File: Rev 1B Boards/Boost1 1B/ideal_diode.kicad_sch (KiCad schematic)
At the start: 6 parts, among them Q1 BSC059N04LS6, U1 LM74700

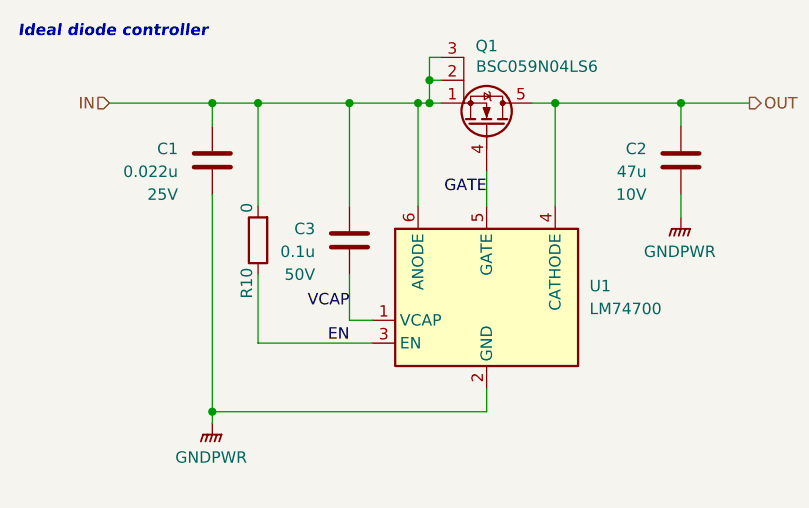
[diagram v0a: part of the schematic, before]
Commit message: Placed footprints for boost stage 1 layout
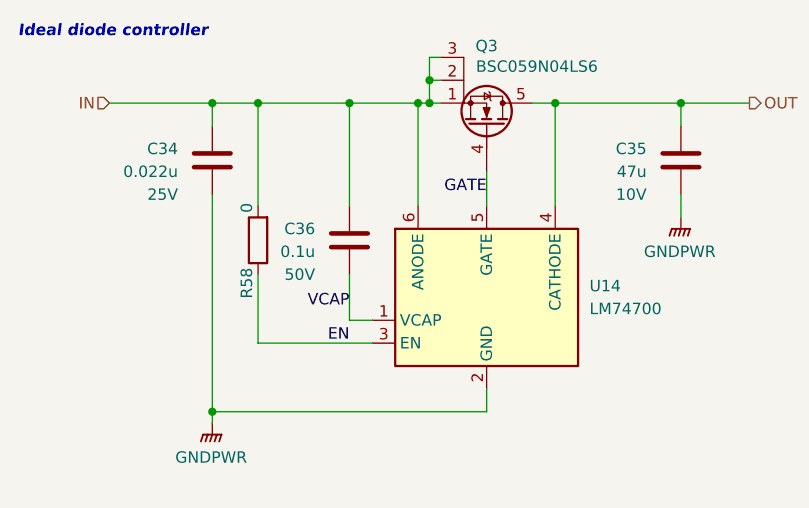
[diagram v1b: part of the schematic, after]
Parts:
- removed R10: 0, Resistor_SMD:R_0603_1608Metric_Pad0.98x0.95mm_HandSolder, symbol Device:R
- added R58: 0, Resistor_SMD:R_0603_1608Metric_Pad0.98x0.95mm_HandSolder, symbol Device:R
- renumbered C1 to C34, C2 to C35, C3 to C36, Q1 to Q3, U1 to U14
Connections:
- net EN: now also R58.1
- net IN: now also R58.2
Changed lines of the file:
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@@
+	(wire
+		(pts
+			(xy 78.74 43.18) (xy 78.74 31.75)
+		)
+		(stroke
+			(width 0)
+			(type default)
+		)
+	)
 	(wire
 		(pts
 			(xy 109.22 31.75) (xy 111.76 31.75)
-		)
-		(stroke
-			(width 0)
-			(type default)
-		)
-	)
-	(wire
-		(pts
-			(xy 78.74 43.18) (xy 78.74 31.75)
 		)
 		(stroke
@@
 			(font
 				(size 1.27 1.27)
+				(thickness 0.1588)
 			)
 			(justify right bottom)
@@
 		(on_board yes)
 		(dnp no)
-		(property "Reference" "C2"
+		(property "Reference" "C35"
 			(at 121.92 36.8299 0)
 			(effects
@@
 		)
 		(instances
-			(project "Ideal Diode Rev1"
-				(path "/1958bbb1-b715-4a10-a229-bee0eabb28b0/4a024d55-f91f-4b32-882f-0df7d5ec96e3"
-					(reference "C3")
-					(unit 1)
-				)
-			)
-			(project "Ideal Diode Rev1"
-				(path "/6197145b-e7d4-44cc-9d90-537b6501bf60/130ec867-c4fa-4318-bea9-b8fc517d0b0a"
-					(reference "C78")
-					(unit 1)
-				)
-			)
 			(project "Buck1 1B"
 				(path "/80afba09-f71a-481c-a343-2cbd993e7569/435402b6-45a2-41c3-bc2a-be9f3f280d73"
-					(reference "C2")
-					(unit 1)
-				)
-			)
-			(project "Rev 1B"
-				(path "/e5f99deb-ef42-4c5f-b80a-388477910e20/7bf219df-2692-4f86-9971-baba03c19447"
 					(reference "C35")
 					(unit 1)
@@
 		(on_board yes)
 		(dnp no)
-		(property "Reference" "C1"
+		(property "Reference" "C34"
 			(at 69.85 36.8299 0)
 			(effects
@@
 		)
 		(instances
-			(project "Ideal Diode Rev1"
-				(path "/1958bbb1-b715-4a10-a229-bee0eabb28b0/4a024d55-f91f-4b32-882f-0df7d5ec96e3"
-					(reference "C1")
-					(unit 1)
-				)
-			)
-			(project "Ideal Diode Rev1"
-				(path "/6197145b-e7d4-44cc-9d90-537b6501bf60/130ec867-c4fa-4318-bea9-b8fc517d0b0a"
-					(reference "C77")
-					(unit 1)
-				)
-			)
 			(project "Buck1 1B"
 				(path "/80afba09-f71a-481c-a343-2cbd993e7569/435402b6-45a2-41c3-bc2a-be9f3f280d73"
-					(reference "C1")
-					(unit 1)
-				)
-			)
-			(project "Rev 1B"
-				(path "/e5f99deb-ef42-4c5f-b80a-388477910e20/7bf219df-2692-4f86-9971-baba03c19447"
 					(reference "C34")
 					(unit 1)
@@
 		(dnp no)
 		(fields_autoplaced yes)
-		(property "Reference" "#PWR03"
+		(property "Reference" "#PWR095"
 			(at 73.66 72.39 0)
 			(effects
@@
 		)
 		(instances
-			(project "Ideal Diode Rev1"
-				(path "/1958bbb1-b715-4a10-a229-bee0eabb28b0/4a024d55-f91f-4b32-882f-0df7d5ec96e3"
-					(reference "#PWR0107")
-					(unit 1)
-				)
-			)
-			(project "Ideal Diode Rev1"
-				(path "/6197145b-e7d4-44cc-9d90-537b6501bf60/130ec867-c4fa-4318-bea9-b8fc517d0b0a"
-					(reference "#PWR0104")
-					(unit 1)
-				)
-			)
 			(project "Buck1 1B"
 				(path "/80afba09-f71a-481c-a343-2cbd993e7569/435402b6-45a2-41c3-bc2a-be9f3f280d73"
-					(reference "#PWR03")
-					(unit 1)
-				)
-			)
-			(project "Rev 1B"
-				(path "/e5f99deb-ef42-4c5f-b80a-388477910e20/7bf219df-2692-4f86-9971-baba03c19447"
 					(reference "#PWR095")
 					(unit 1)
@@
 		(on_board yes)
 		(dnp no)
-		(property "Reference" "C3"
+		(property "Reference" "C36"
 			(at 85.09 45.7199 0)
 			(effects
@@
 		)
 		(instances
-			(project "Ideal Diode Rev1"
-				(path "/1958bbb1-b715-4a10-a229-bee0eabb28b0/4a024d55-f91f-4b32-882f-0df7d5ec96e3"
-					(reference "C2")
-					(unit 1)
-				)
-			)
-			(project "Ideal Diode Rev1"
-				(path "/6197145b-e7d4-44cc-9d90-537b6501bf60/130ec867-c4fa-4318-bea9-b8fc517d0b0a"
-					(reference "C79")
-					(unit 1)
-				)
-			)
 			(project "Buck1 1B"
 				(path "/80afba09-f71a-481c-a343-2cbd993e7569/435402b6-45a2-41c3-bc2a-be9f3f280d73"
-					(reference "C3")
-					(unit 1)
-				)
-			)
-			(project "Rev 1B"
-				(path "/e5f99deb-ef42-4c5f-b80a-388477910e20/7bf219df-2692-4f86-9971-baba03c19447"
 					(reference "C36")
 					(unit 1)
@@
 		(on_board yes)
 		(dnp no)
-		(property "Reference" "Q1"
+		(property "Reference" "Q3"
 			(at 104.14 25.4 90)
 			(effects
@@
 		)
 		(instances
-			(project "Ideal Diode Rev1"
-				(path "/1958bbb1-b715-4a10-a229-bee0eabb28b0/4a024d55-f91f-4b32-882f-0df7d5ec96e3"
-					(reference "Q1")
-					(unit 1)
-				)
-			)
-			(project "Ideal Diode Rev1"
-				(path "/6197145b-e7d4-44cc-9d90-537b6501bf60/130ec867-c4fa-4318-bea9-b8fc517d0b0a"
-					(reference "Q11")
-					(unit 1)
-				)
-			)
 			(project "Buck1 1B"
 				(path "/80afba09-f71a-481c-a343-2cbd993e7569/435402b6-45a2-41c3-bc2a-be9f3f280d73"
-					(reference "Q1")
-					(unit 1)
-				)
-			)
-			(project "Rev 1B"
-				(path "/e5f99deb-ef42-4c5f-b80a-388477910e20/7bf219df-2692-4f86-9971-baba03c19447"
 					(reference "Q3")
 					(unit 1)
@@
 		(dnp no)
 		(fields_autoplaced yes)
-		(property "Reference" "U1"
+		(property "Reference" "U14"
 			(at 115.57 52.0699 0)
 			(effects
@@
 		)
 		(instances
-			(project "Ideal Diode Rev1"
-				(path "/1958bbb1-b715-4a10-a229-bee0eabb28b0/4a024d55-f91f-4b32-882f-0df7d5ec96e3"
-					(reference "U2")
-					(unit 1)
-				)
-			)
-			(project "Ideal Diode Rev1"
-				(path "/6197145b-e7d4-44cc-9d90-537b6501bf60/130ec867-c4fa-4318-bea9-b8fc517d0b0a"
-					(reference "U18")
-					(unit 1)
-				)
-			)
 			(project "Buck1 1B"
 				(path "/80afba09-f71a-481c-a343-2cbd993e7569/435402b6-45a2-41c3-bc2a-be9f3f280d73"
-					(reference "U1")
-					(unit 1)
-				)
-			)
-			(project "Rev 1B"
-				(path "/e5f99deb-ef42-4c5f-b80a-388477910e20/7bf219df-2692-4f86-9971-baba03c19447"
 					(reference "U14")
 					(unit 1)
@@
 		(dnp no)
 		(fields_autoplaced yes)
-		(property "Reference" "#PWR02"
+		(property "Reference" "#PWR094"
 			(at 125.73 49.53 0)
 			(effects
@@
 		)
 		(instances
-			(project "Ideal Diode Rev1"
-				(path "/1958bbb1-b715-4a10-a229-bee0eabb28b0/4a024d55-f91f-4b32-882f-0df7d5ec96e3"
-					(reference "#PWR0104")
-					(unit 1)
-				)
-			)
-			(project "Ideal Diode Rev1"
-				(path "/6197145b-e7d4-44cc-9d90-537b6501bf60/130ec867-c4fa-4318-bea9-b8fc517d0b0a"
-					(reference "#PWR0103")
-					(unit 1)
-				)
-			)
 			(project "Buck1 1B"
 				(path "/80afba09-f71a-481c-a343-2cbd993e7569/435402b6-45a2-41c3-bc2a-be9f3f280d73"
-					(reference "#PWR02")
-					(unit 1)
-				)
-			)
-			(project "Rev 1B"
-				(path "/e5f99deb-ef42-4c5f-b80a-388477910e20/7bf219df-2692-4f86-9971-baba03c19447"
 					(reference "#PWR094")
 					(unit 1)
@@
 		(on_board yes)
 		(dnp no)
-		(property "Reference" "R10"
+		(property "Reference" "R58"
 			(at 78.232 50.038 90)
 			(effects
@@
 		)
 		(instances
-			(project "SupercapManager"
-				(path "/6197145b-e7d4-44cc-9d90-537b6501bf60/130ec867-c4fa-4318-bea9-b8fc517d0b0a"
-					(reference "R2")
+			(project "Buck1 1B"
+				(path "/80afba09-f71a-481c-a343-2cbd993e7569/435402b6-45a2-41c3-bc2a-be9f3f280d73"
+					(reference "R58")
 					(unit 1)
 				)
-			)
-			(project "Boost1 1B"
-				(path "/80afba09-f71a-481c-a343-2cbd993e7569/435402b6-45a2-41c3-bc2a-be9f3f280d73"
-					(reference "R10")
-					(unit 1)
-				)
